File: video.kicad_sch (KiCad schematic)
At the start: 52 parts, among them CN103 RF Modulator, IC103 HUC6260, IC108 μPC358C

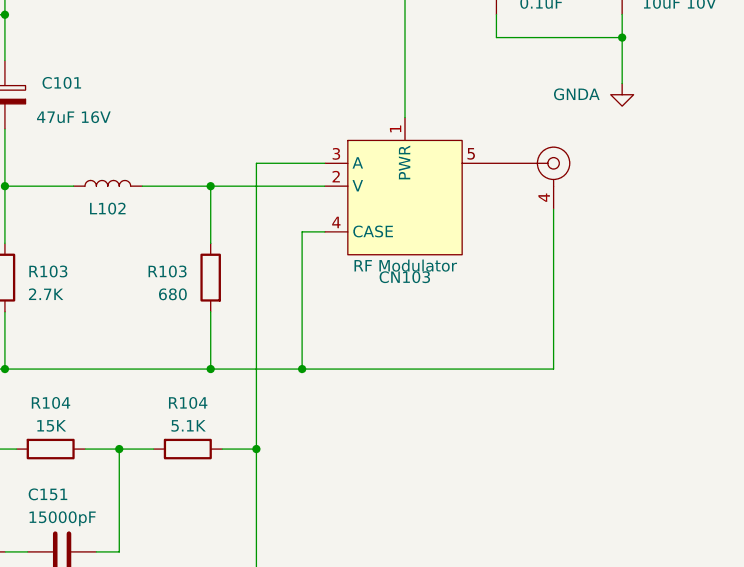
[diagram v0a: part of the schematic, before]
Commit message: Inductor symbol for L101, schematic layout clean-up.
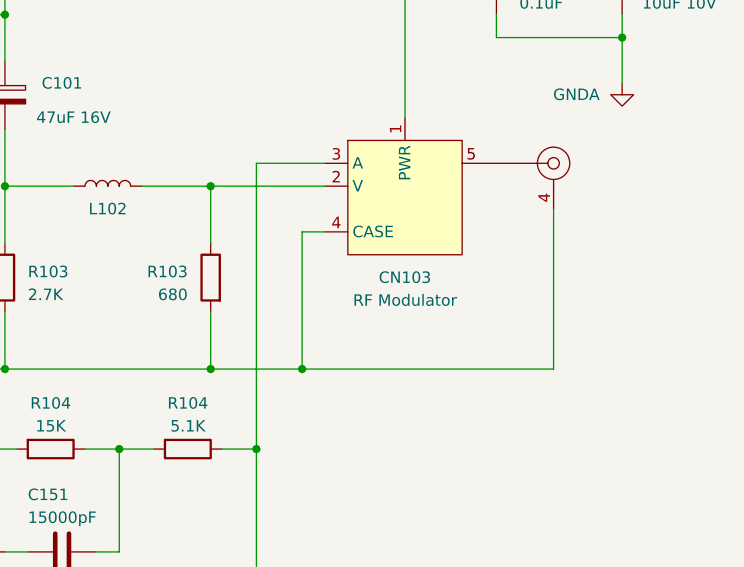
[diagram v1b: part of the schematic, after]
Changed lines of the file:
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@@
   (title_block
     (title "PC Engine Video Encoding")
-    (date "2023-09-18")
-    (rev "1.1")
+    (date "2023-09-20")
+    (rev "1.2")
     (comment 1 "Differences reverse engineered from original PWD-623A board")
     (comment 2 "Adapted from existing TurboGrafx-16 schematics by Cosam")
@@
   )
   (symbol (lib_id "PC-Engine:RF_Modulator") (at 328.93 129.54 0) (unit 1)
-    (in_bom yes) (on_board yes) (dnp no) (fields_autoplaced)
+    (in_bom yes) (on_board yes) (dnp no)
     (property "Reference" "CN103" (at 328.93 130.81 0)
       (effects (font (size 1.27 1.27)))
     )
-    (property "Value" "RF Modulator" (at 328.93 129.54 0)
+    (property "Value" "RF Modulator" (at 328.93 133.35 0)
       (effects (font (size 1.27 1.27)))
     )

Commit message: Add contact info the schematics for publishing.
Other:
- company: (none) -> By Cosam
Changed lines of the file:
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@@
   (title_block
     (title "PC Engine Video Encoding")
-    (date "2023-09-20")
-    (rev "1.2")
-    (comment 1 "Differences reverse engineered from original PWD-623A board")
-    (comment 2 "Adapted from existing TurboGrafx-16 schematics by Cosam")
+    (date "2023-11-15")
+    (rev "1.2.1")
+    (company "By Cosam")
+    (comment 1 "https://github.com/Board-Folk/PC-Engine")
+    (comment 2 "For contributions or corrections please visit:")
+    (comment 3 "Differences reverse engineered from original PWD-623A board")
+    (comment 4 "Adapted from existing TurboGrafx-16 schematics")
   )
   (junction (at 210.82 144.78) (diameter 0) (color 0 0 0 0)
